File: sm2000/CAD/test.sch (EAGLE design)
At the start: 30 parts, among them Q1 BRF92, Q2 BFQ19, Q3 BFQ19, X1 BU-SMA-G, X2 BU-SMA-G

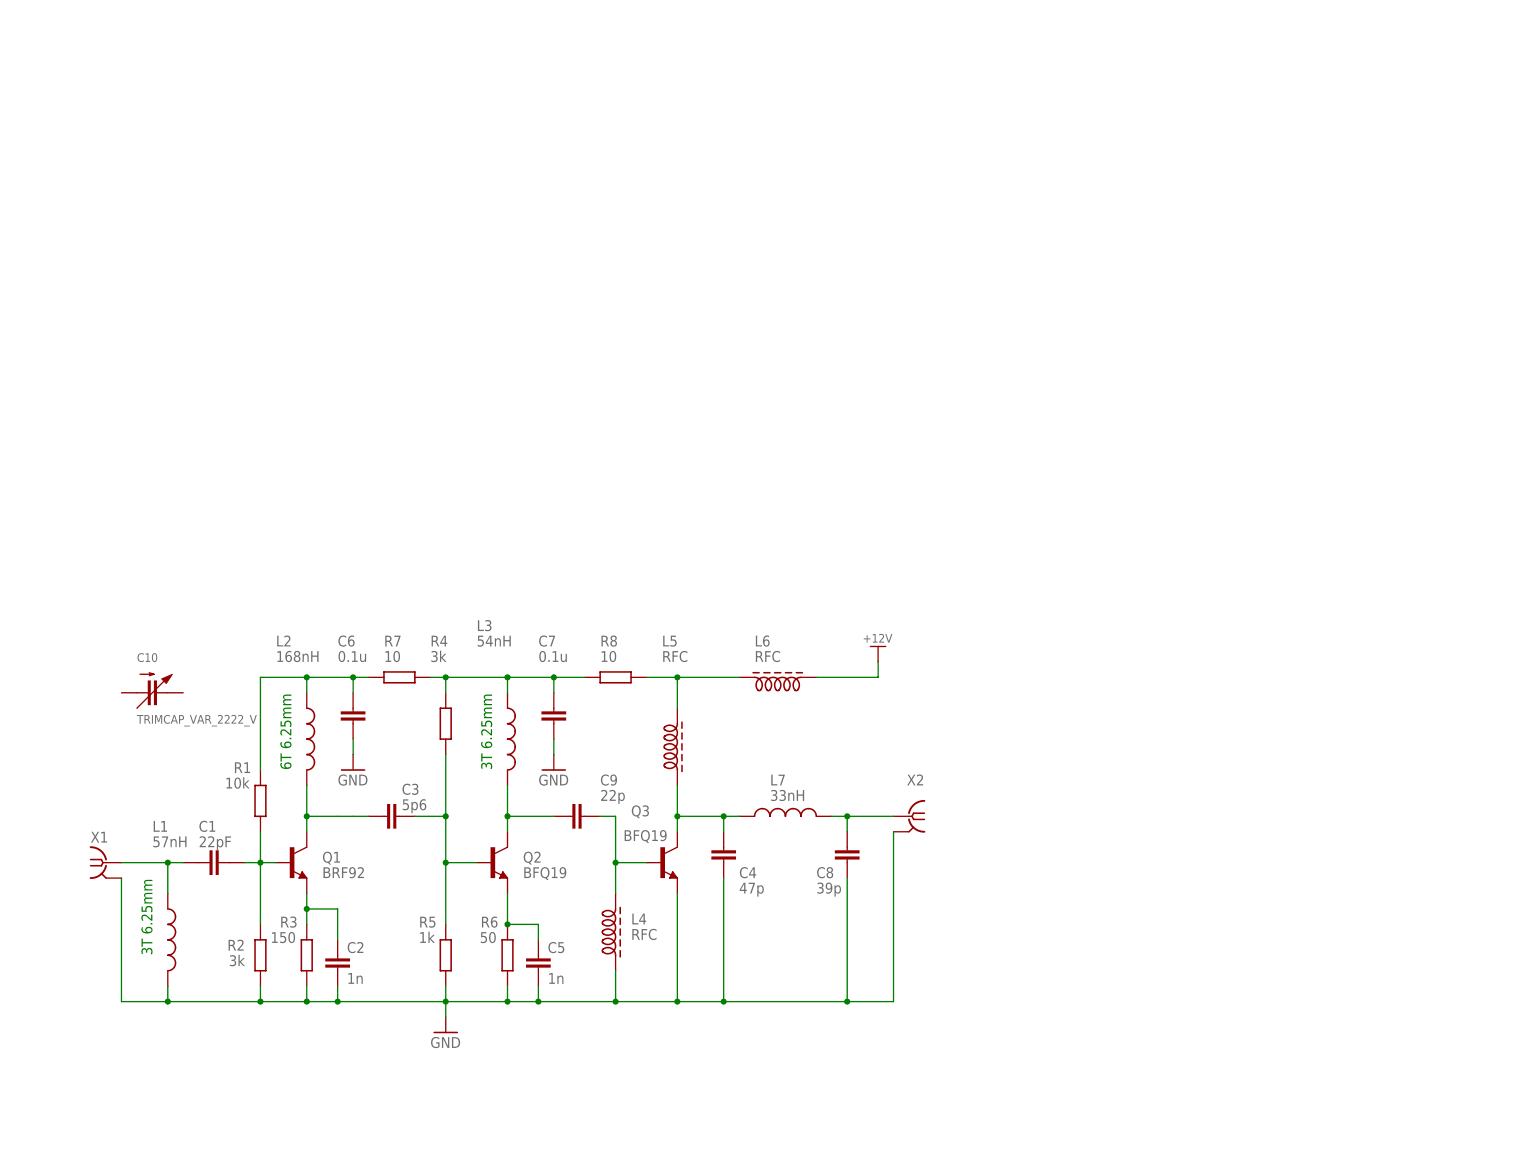
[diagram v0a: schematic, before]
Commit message: Update schematic & PCB RGB
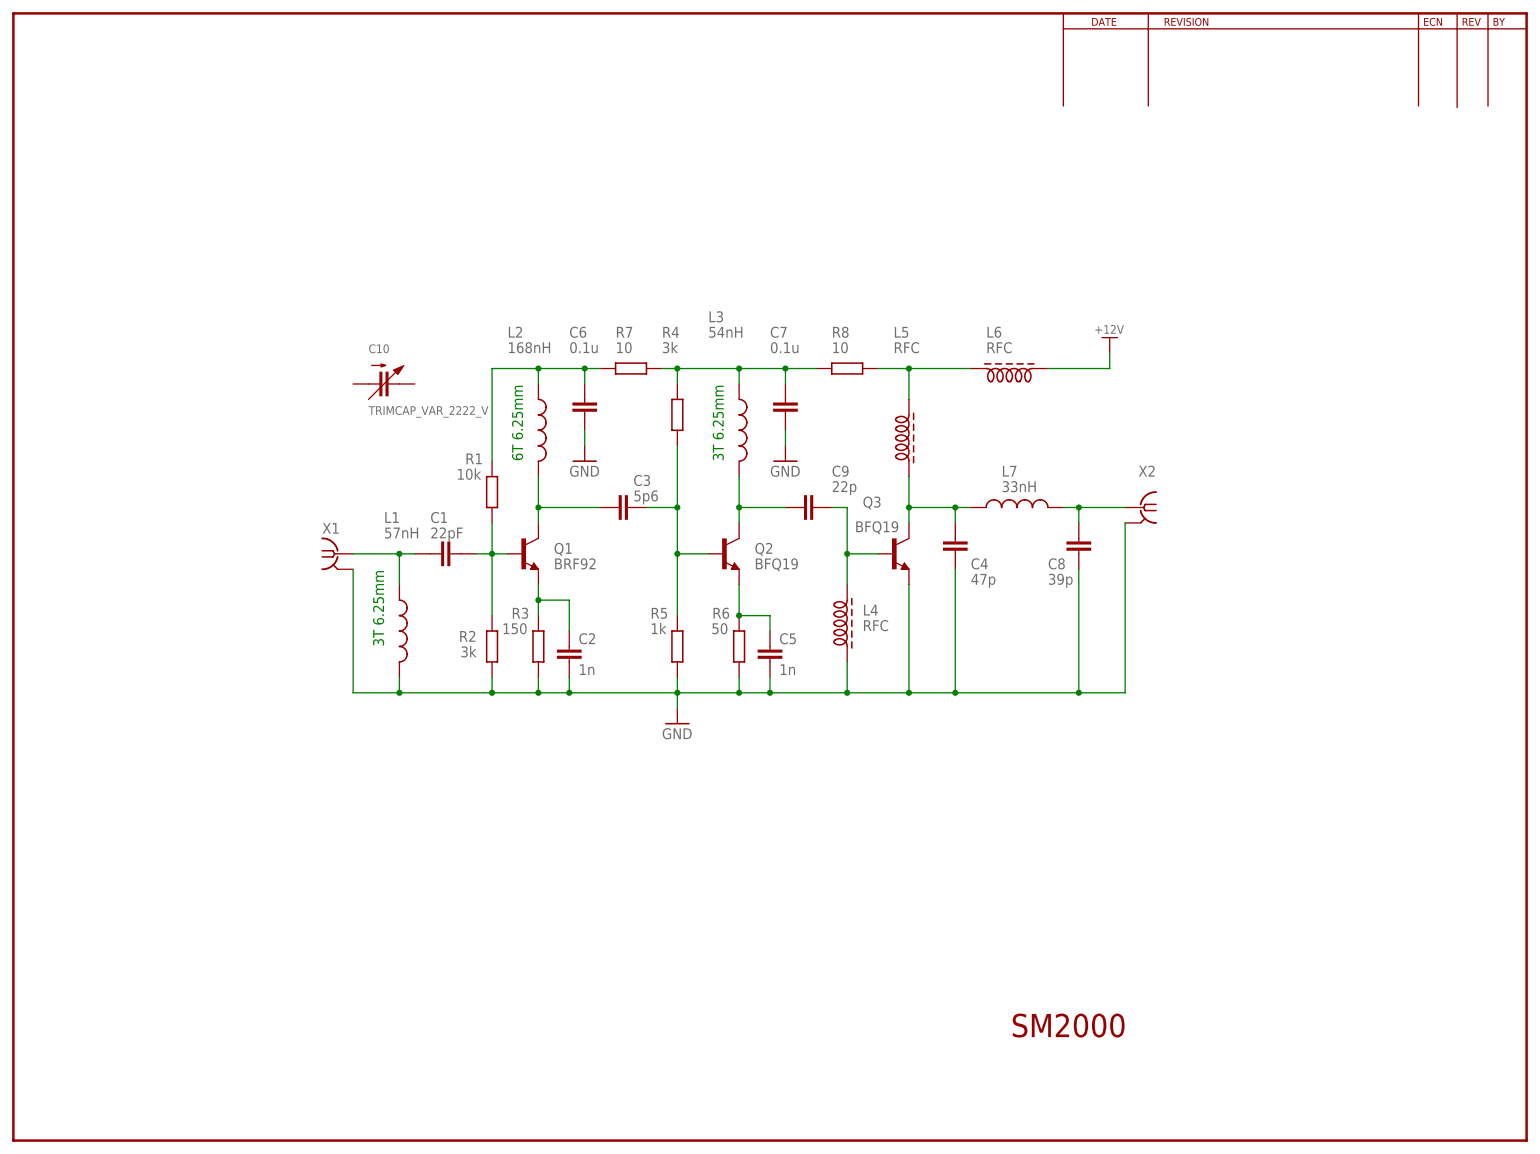
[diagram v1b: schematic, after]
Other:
- note added: "SM2000"
- moved on the sheet: C1, C10, C2, C3, C4, C5, C6, C7, C8, C9, L1, L2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

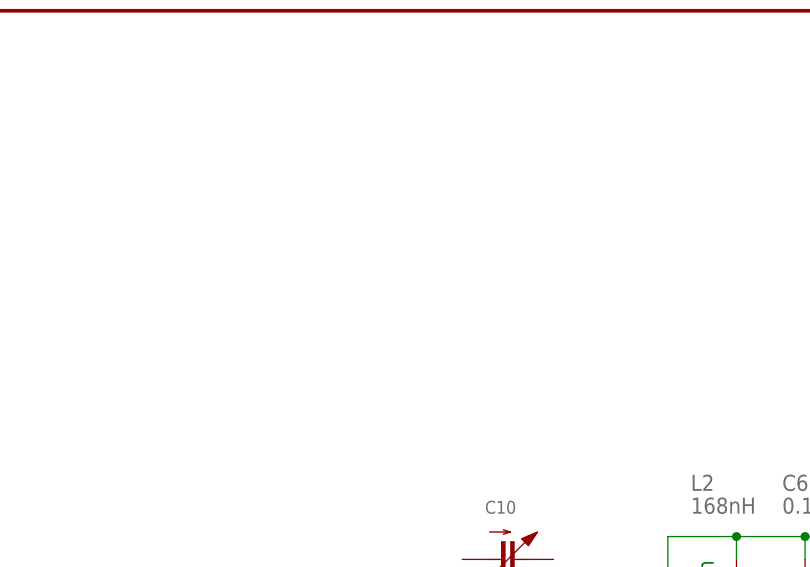
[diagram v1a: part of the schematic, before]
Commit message: Add rowetel.lbr with new SM2000 components. RGB
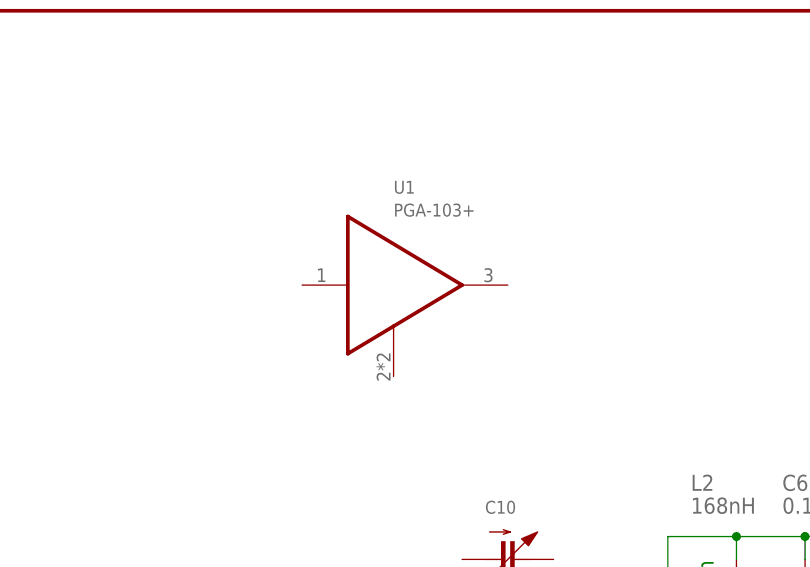
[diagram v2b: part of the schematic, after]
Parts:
- added U1: PGA-103+, _RoweTel:PGA-103+
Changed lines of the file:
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@@
 <part name="C10" library="_RoweTel" deviceset="TRIMCAP_VAR_2222_V" device=""/>
 <part name="U$1" library="A-FRAMES" deviceset="ROWE-ASIZE" device=""/>
+<part name="U1" library="_RoweTel" deviceset="PGA-103+" device=""/>
 </parts>
 <sheets>
@@
 <instance part="U$1" gate="G$2" x="147.32" y="0"/>
 <instance part="U$1" gate="G$3" x="175.26" y="185.42"/>
+<instance part="U1" gate="G$1" x="48.26" y="154.94"/>
 </instances>
 <busses>
